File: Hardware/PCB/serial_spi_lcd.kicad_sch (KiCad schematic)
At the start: 0 parts

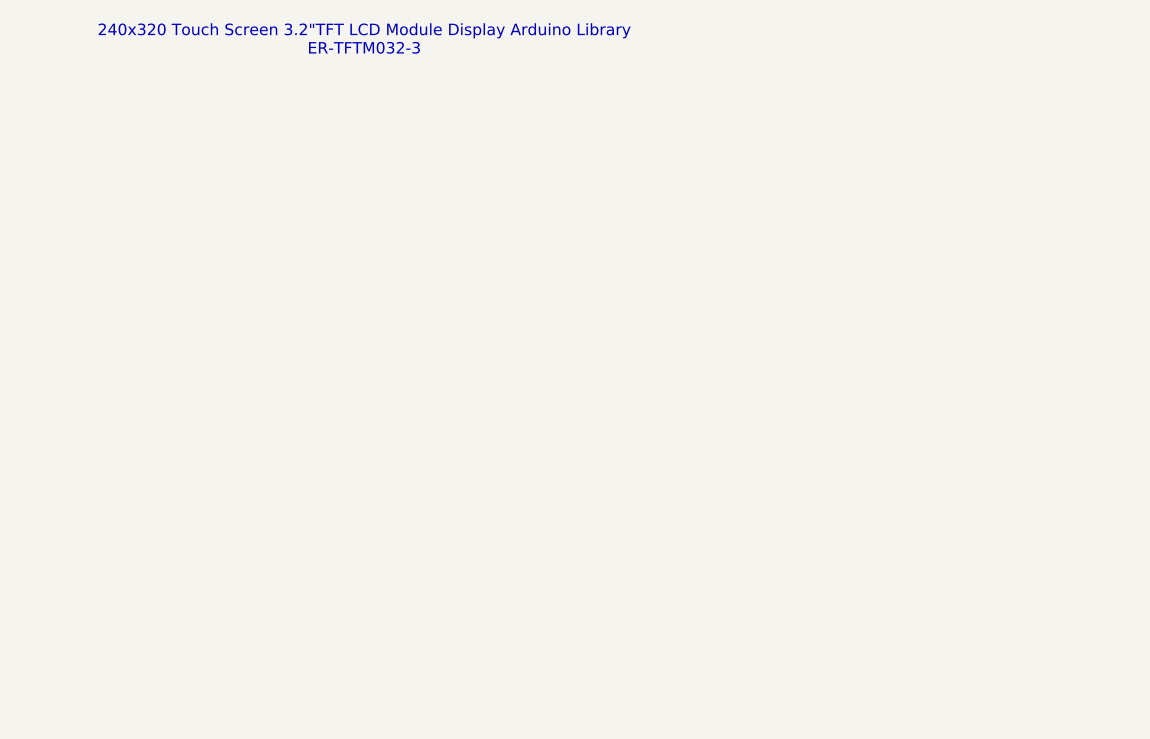
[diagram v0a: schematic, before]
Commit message: added symbol for LCD, working on adding PWM output terminal for brushless pump motors
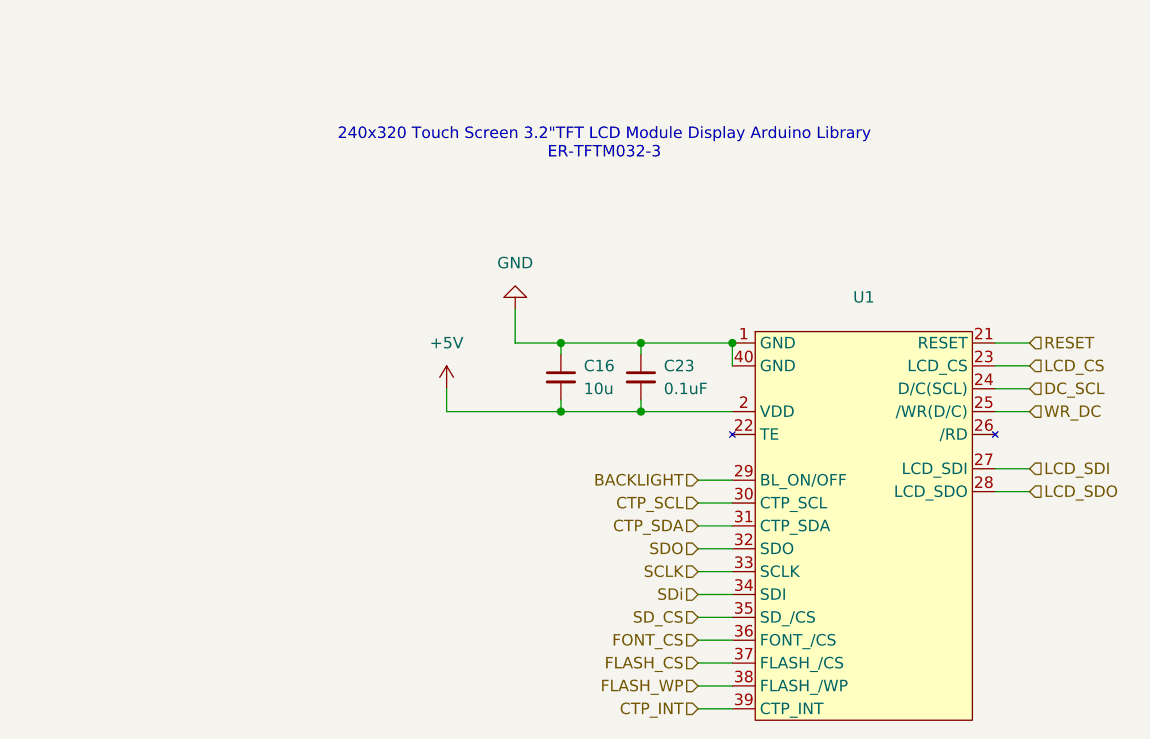
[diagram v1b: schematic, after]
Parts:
- added C16: 10u, Capacitor_SMD:C_0805_2012Metric_Pad1.18x1.45mm_HandSolder, symbol Device:C_Small
- added C23: 0.1uF, Capacitor_SMD:C_0603_1608Metric_Pad1.08x0.95mm_HandSolder, symbol Device:C_Small
- added U1: ~, Vendor_Footprints:GCT_FFC3B07-40-T, symbol Vendor_Symbols:ER-TFTM032-3
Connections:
- new net: U1.10 (DB7), U1.11 (DB8), U1.12 (DB9), U1.13 (DB10), U1.14 (DB11), U1.15 (DB12), U1.16 (DB13), U1.17 (DB14), U1.18 (DB15), U1.19 (NC), U1.20 (NC), U1.3 (DB0), U1.4 (DB1), U1.5 (DB2), U1.6 (DB3), U1.7 (DB4), U1.8 (DB5), U1.9 (DB6)
- new net +5V: C16.2, C23.2, U1.2 (VDD)
- new net BACKLIGHT: U1.29 (BL_ON/OFF)
- new net CTP_INT: U1.39 (CTP_INT)
- new net CTP_SCL: U1.30 (CTP_SCL)
- new net CTP_SDA: U1.31 (CTP_SDA)
- new net DC_SCL: U1.24 (D/C(SCL))
- new net FLASH_CS: U1.37 (FLASH_/CS)
- new net FLASH_WP: U1.38 (FLASH_/WP)
- new net FONT_CS: U1.36 (FONT_/CS)
- new net GND: C16.1, C23.1, U1.1 (GND), U1.40 (GND)
- new net LCD_CS: U1.23 (LCD_CS)
- new net LCD_SDI: U1.27 (LCD_SDI)
- new net LCD_SDO: U1.28 (LCD_SDO)
- new net RESET: U1.21 (RESET)
- new net SCLK: U1.33 (SCLK)
- new net SDO: U1.32 (SDO)
- new net SD_CS: U1.35 (SD_/CS)
- new net SDi: U1.34 (SDI)
- new net WR_DC: U1.25 (/WR(D/C))

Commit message: Added brushless DC support, fixed terminal blocks too
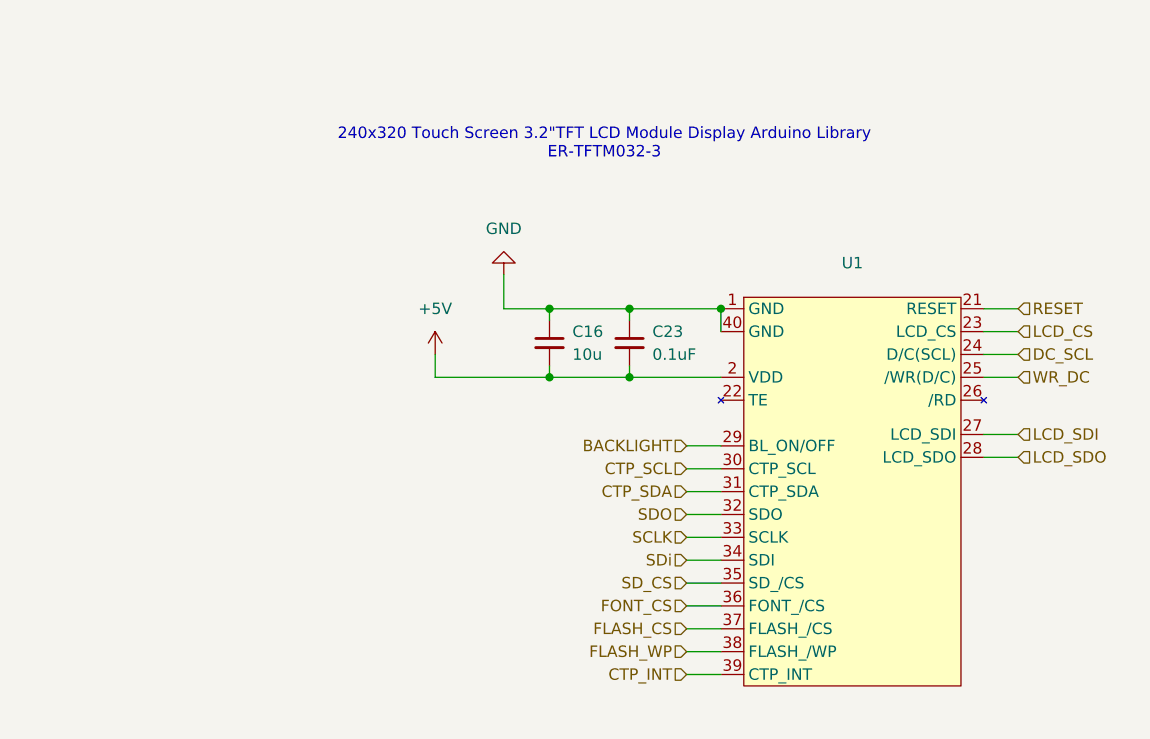
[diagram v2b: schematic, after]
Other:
- moved on the sheet: C16, C23, U1

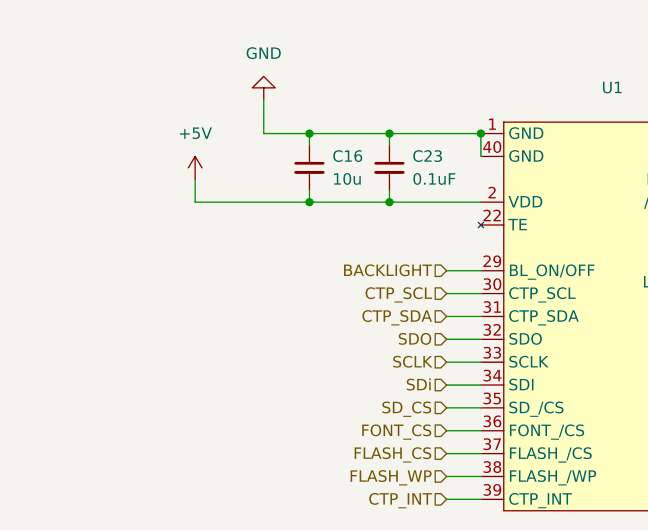
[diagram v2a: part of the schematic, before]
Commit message: switched to making buck converter to save costs and space, and to allow for LDO after 5.5V for better stability
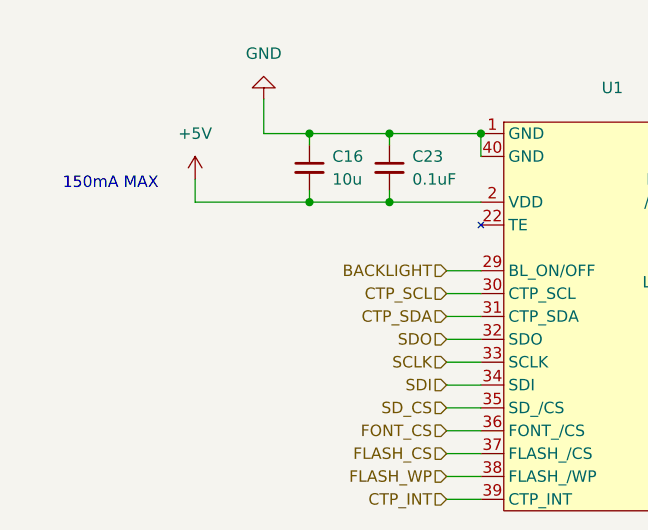
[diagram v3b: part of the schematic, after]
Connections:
- net SDi renamed SDI
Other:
- note added: "150mA MAX"

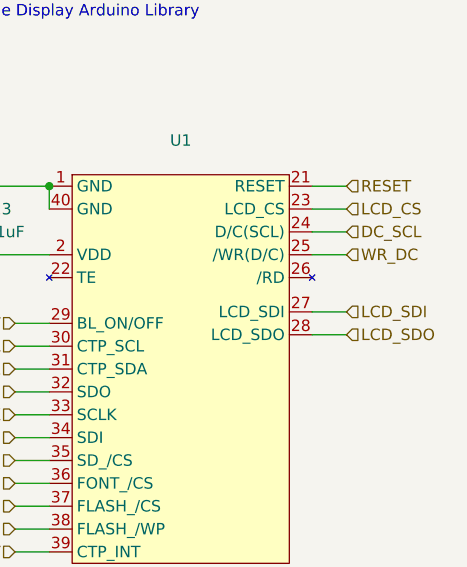
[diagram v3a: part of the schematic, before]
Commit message: consolidated IO for LCD block, broke out hierarchial pins, need to start wiring everything up and then on to layout
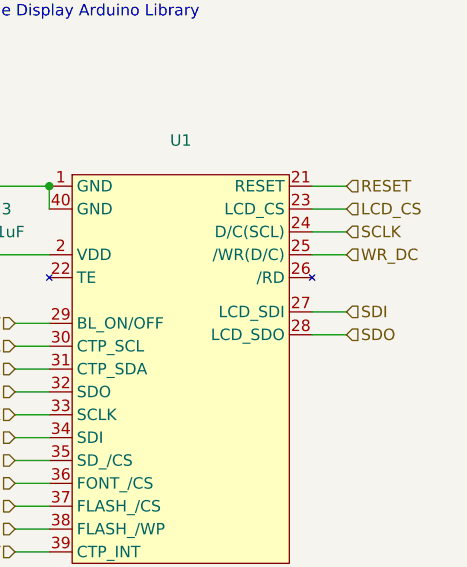
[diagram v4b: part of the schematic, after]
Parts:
- U1: DigiKey Link (none) -> https://www.digikey.com/en/products/detail/gct/FFC3B07-40-T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; MPN (none) -> FFC3B07-40-T; Manufacturer (none) -> GCT
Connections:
- net DC_SCL is gone; now on net SCLK: U1.24 (D/C(SCL))
- net LCD_SDI is gone; now on net SDI: U1.27 (LCD_SDI)
- net LCD_SDO is gone; now on net SDO: U1.28 (LCD_SDO)
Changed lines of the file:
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@@
+		)
+	)
+	(hierarchical_label "SCLK"
+		(shape input)
+		(at 123.19 55.88 0)
+		(effects
+			(font
+				(size 1.27 1.27)
+			)
+			(justify left)
 		)
 	)
@@
 		)
 	)
-	(hierarchical_label "LCD_SDO"
+	(hierarchical_label "BACKLIGHT"
+		(shape input)
+		(at 86.36 66.04 180)
+		(effects
+			(font
+				(size 1.27 1.27)
+			)
+			(justify right)
+		)
+	)
+	(hierarchical_label "FLASH_WP"
+		(shape input)
+		(at 86.36 88.9 180)
+		(effects
+			(font
+				(size 1.27 1.27)
+			)
+			(justify right)
+		)
+	)
+	(hierarchical_label "SD_CS"
+		(shape input)
+		(at 86.36 81.28 180)
+		(effects
+			(font
+				(size 1.27 1.27)
+			)
+			(justify right)
+		)
+	)
+	(hierarchical_label "CTP_SDA"
+		(shape input)
+		(at 86.36 71.12 180)
+		(effects
+			(font
+				(size 1.27 1.27)
+			)
+			(justify right)
+		)
+	)
+	(hierarchical_label "SDO"
 		(shape input)
 		(at 123.19 67.31 0)
@@
 		)
 	)
-	(hierarchical_label "BACKLIGHT"
-		(shape input)
-		(at 86.36 66.04 180)
-		(effects
-			(font
-				(size 1.27 1.27)
-			)
-			(justify right)
-		)
-	)
-	(hierarchical_label "FLASH_WP"
-		(shape input)
-		(at 86.36 88.9 180)
-		(effects
-			(font
-				(size 1.27 1.27)
-			)
-			(justify right)
-		)
-	)
-	(hierarchical_label "SD_CS"
-		(shape input)
-		(at 86.36 81.28 180)
-		(effects
-			(font
-				(size 1.27 1.27)
-			)
-			(justify right)
-		)
-	)
-	(hierarchical_label "CTP_SDA"
-		(shape input)
-		(at 86.36 71.12 180)
-		(effects
-			(font
-				(size 1.27 1.27)
-			)
-			(justify right)
+	(hierarchical_label "SDI"
+		(shape input)
+		(at 123.19 64.77 0)
+		(effects
+			(font
+				(size 1.27 1.27)
+			)
+			(justify left)
 		)
 	)
@@
 			)
 			(justify right)
-		)
-	)
-	(hierarchical_label "LCD_SDI"
-		(shape input)
-		(at 123.19 64.77 0)
-		(effects
-			(font
-				(size 1.27 1.27)
-			)
-			(justify left)
-		)
-	)
-	(hierarchical_label "DC_SCL"
-		(shape input)
-		(at 123.19 55.88 0)
-		(effects
-			(font
-				(size 1.27 1.27)
-			)
-			(justify left)
 		)
 	)
@@
 			)
 		)
-		(property "Description" ""
+		(property "Description" "40 Position FFC, FPC Connector Contacts, Bottom 0.039\" (1.00mm) Surface Mount, Right Angle"
 			(at 92.71 50.8 0)
 			(effects
 				(font
+					(size 1.27 1.27)
+				)
+				(hide yes)
+			)
+		)
+		(property "MPN" "FFC3B07-40-T"
+			(at 104.14 49.53 0)
+			(effects
+				(font
+					(size 1.27 1.27)
+				)
+				(hide yes)
+			)
+		)
+		(property "Manufacturer" "GCT"
+			(at 104.14 49.53 0)
+			(effects
+				(font
+					(size 1.27 1.27)
+				)
+				(hide yes)
+			)
+		)
+		(property "DigiKey Link" "https://www.digikey.com/en/products/detail/gct/FFC3B07-40-T/10656983"
+			(at 104.14 49.53 0)
+			(effects
+				(font
+					(size 1.27 1.27)
+				)
+				(hide yes)
+			)
+		)
+		(property "Mouser Link" ""
+			(at 104.14 49.53 0)
+			(effects
+				(font

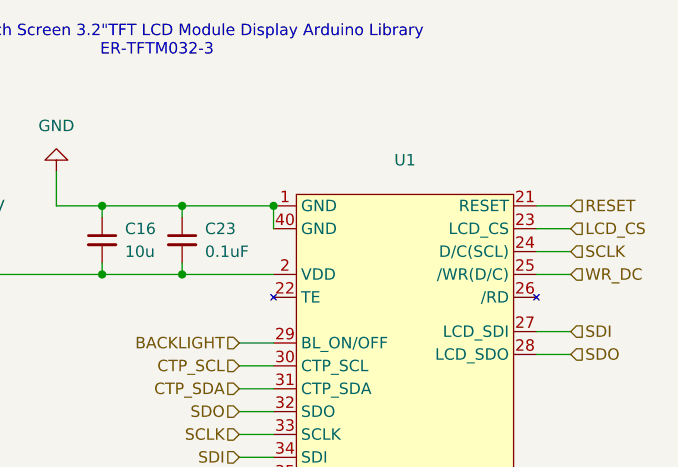
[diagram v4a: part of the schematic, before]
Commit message: overall design is pretty much done, starting layout and routing now
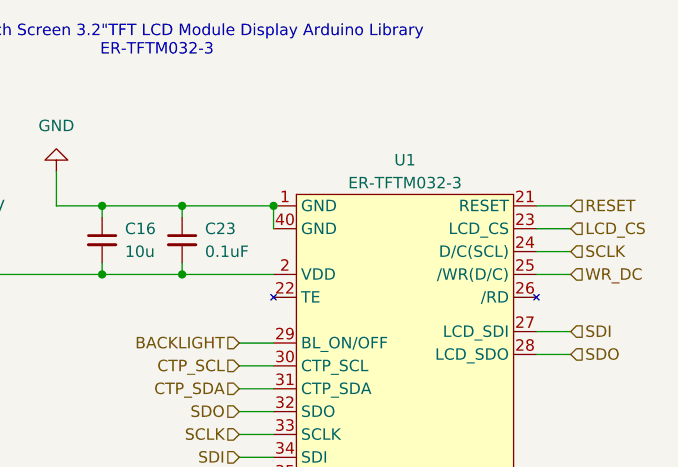
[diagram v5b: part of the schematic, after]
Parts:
- U1: value ~ -> ER-TFTM032-3

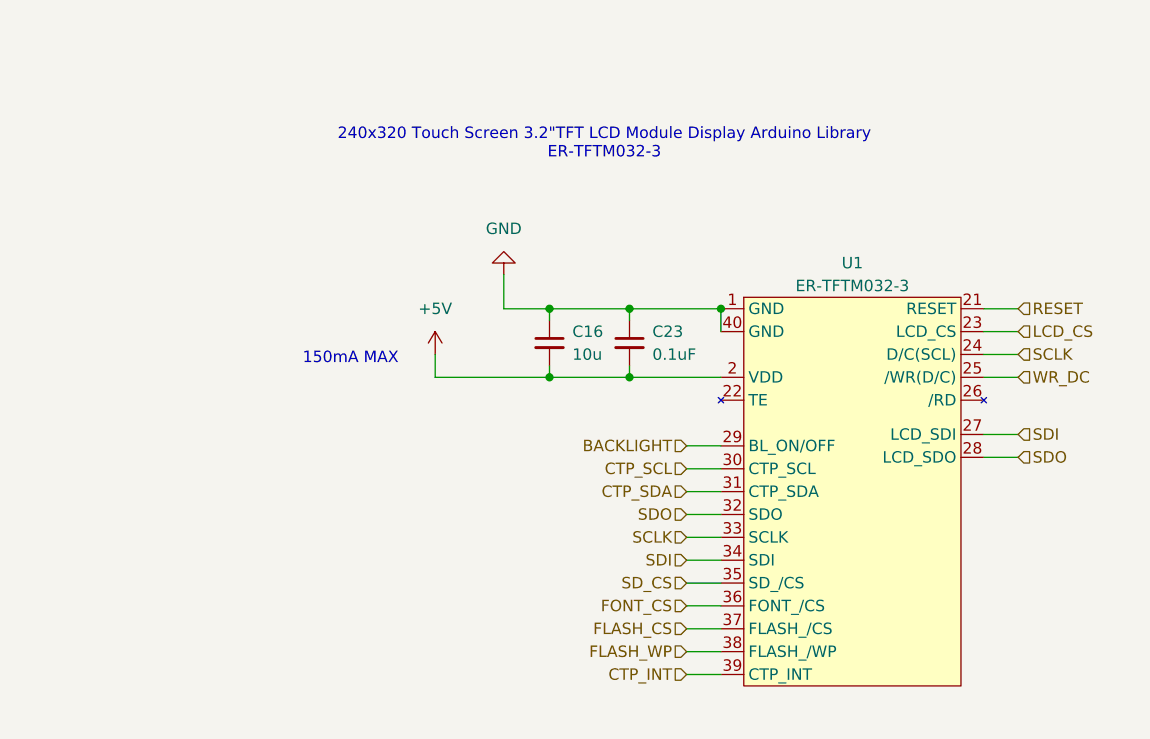
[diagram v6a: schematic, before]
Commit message: fixed BOM, added some silkscreen, getting quote now
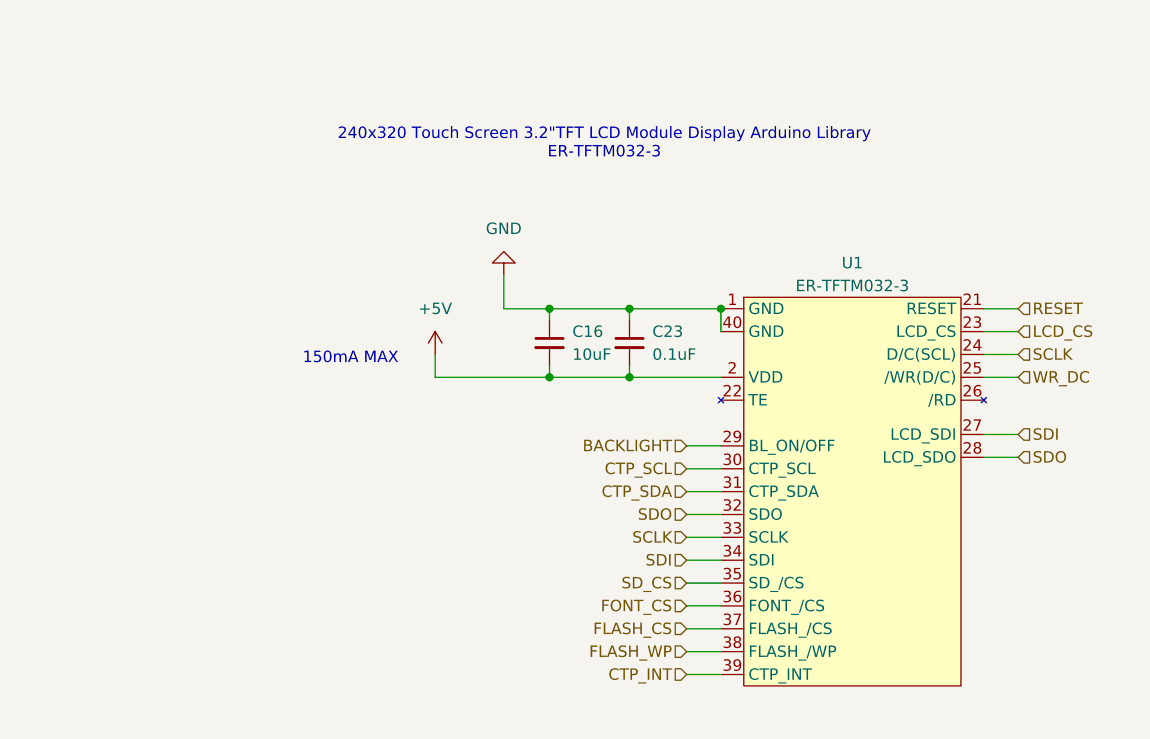
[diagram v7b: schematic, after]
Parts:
- C16: value 10u -> 10uF
- C23: DigiKey Link (none) -> https://www.digikey.com/en/products/detail/samsung-electro-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; MPN GCM188R71H104KA57J -> CL10B104KO8NNNC; Manufacturer (none) -> Samsung Electro-Mechanics
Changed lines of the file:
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@@
 			"AHoAdQBnAHIAWQB6AC8AVwBHACsAYgBoAEYANgBGAGoAMQA3ADEAMQArAGoAcQBOADgAZQBRAHcA"
 			"ZQBaAFEASQAxAGIAQQAzADEAWABiAE0ASAAyAEkAeQA1AFkAWgBYAHcAWABzAC8AdQBPAHgAZgBG"
-			"AFAAZwBxAE8ANQBsAEQAYQBhAEQAKwAwAEoAQQA0AG4AcwBzAFoAQQBLAGwAWABnAA=="
+			"AFAAZwBxAE8ANQBsAEQAYQBhAEQAKwAwAEoAQQA0AG4AcwBzAFoAQQBLAGwAWABnAAAAEBs6AXIC"
+			"AACQVToBcgIAAIidSp/7fwAAkLtKn/t/AACInUqf+38AAMBVOgFyAgAAMBs6AXICAAAwvkqf+38A"
+			"AFAbOgFyAgAA8FU6AXICAACInUqf+38AAJC7Sp/7fwAAiJ1Kn/t/AAAgVjoBcgIAAHAbOgFyAgAA"
+			"ML5Kn/t/AACQGzoBcgIAAFBWOgFyAgAAiJ1Kn/t/AACQu0qf+38AAIidSp/7fwAAgFY6AXICAACw"
+			"GzoBcgIAADC+Sp/7fwAA0Bs6AXICAACwVjoBcgIAAIidSp/7fwAAkLtKn/t/AACInUqf+38AAOBW"
+			"OgFyAgAA8Bs6AXICAAAwvkqf+38AABAcOgFyAgAAEFc6AXICAACInUqf+38AAJC7Sp/7fwAAiJ1K"
+			"n/t/AABAVzoBcgIAADAcOgFyAgAAML5Kn/t/AABQHDoBcgIAAHBXOgFyAgAAiJ1Kn/t/AACQu0qf"
+			"+38AAIidSp/7fwAAoFc6AXICAABwHDoBcgIAADC+Sp/7fwAAkBw6AXICAADQVzoBcgIAAIidSp/7"
+			"fwAAkLtKn/t/AACInUqf+38AAABYOgFyAgAAsBw6AXICAAAwvkqf+38AANAcOgFyAgAAMFg6AXIC"
+			"AACInUqf+38AAJC7Sp/7fwAAiJ1Kn/t/AABgWDoBcgIAAPAcOgFyAgAAML5Kn/t/AAAQHToBcgIA"
+			"AJBYOgFyAgAAiJ1Kn/t/AACQu0qf+38AAIidSp/7fwAAwFg6AXICAAAwHToBcgIAADC+Sp/7fwAA"
+			"UB06AXICAADwWDoBcgIAAIidSp/7fwAAkLtKn/t/AACInUqf+38AACBZOgFyAgAAcB06AXICAAAw"
+			"vkqf+38AAJAdOgFyAgAAUFk6AXICAACInUqf+38AAJC7Sp/7fwAAiJ1Kn/t/AACAWToBcgIAALAd"
+			"OgFyAgAAML5Kn/t/AADQHToBcgIAALBZOgFyAgAAiJ1Kn/t/AACQu0qf+38AAIidSp/7fwAA4Fk6"
+			"AXICAADwHToBcgIAADC+Sp/7fwAAEB46AXICAAAQWjoBcgIAAIidSp/7fwAAkLtKn/t/AACInUqf"
+			"+38AAEBaOgFyAgAAMB46AXICAAAwvkqf+38AAFAeOgFyAgAAcFo6AXICAACInUqf+38AAJC7Sp/7"
+			"fwAAiJ1Kn/t/AACgWjoBcgIAAHAeOgFyAgAAML5Kn/t/AACQHjoBcgIAANBaOgFyAgAAiJ1Kn/t/"
+			"AACQu0qf+38AAIidSp/7fwAAAFs6AXICAACwHjoBcgIAADC+Sp/7fwAA0B46AXICAAAwWzoBcgIA"
+			"AIidSp/7fwAAkLtKn/t/AACInUqf+38AAGBbOgFyAgAA8B46AXICAAAwvkqf+38AAA=="
 		)
 	)
@@
 			)
 		)
-		(property "Description" "0.1 µF ±10% 50V Ceramic Capacitor X7R 0603 (1608 Metric)"
-			(at 80.01 54.61 0)
-			(effects
-				(font
-					(size 1.27 1.27)
-				)
-				(hide yes)
-			)
-		)
-		(property "MPN" "GCM188R71H104KA57J"
+		(property "Description" "0.1 µF ±10% 16V Ceramic Capacitor X7R 0603 (1608 Metric)"
+			(at 80.01 54.61 0)
+			(effects
+				(font
+					(size 1.27 1.27)
+				)
+				(hide yes)
+			)
+		)
+		(property "MPN" "CL10B104KO8NNNC"
+			(at 80.01 54.61 0)
+			(effects
+				(font
+					(size 1.27 1.27)
+				)
+				(hide yes)
+			)
+		)
+		(property "DigiKey Link" "https://www.digikey.com/en/products/detail/samsung-electro-mechanics/CL10B104KO8NNNC/3886663"
+			(at 80.01 54.61 0)
+			(effects
+				(font
+					(size 1.27 1.27)
+				)
+				(hide yes)
+			)
+		)
+		(property "Manufacturer" "Samsung Electro-Mechanics"
+			(at 80.01 54.61 0)
+			(effects
+				(font
+					(size 1.27 1.27)
+				)
+				(hide yes)
+			)
+		)
+		(property "Mouser Link" ""
 			(at 80.01 54.61 0)
 			(effects
@@
 			)
 		)
-		(property "Value" "10u"
+		(property "Value" "10uF"
 			(at 73.66 55.8862 0)
 			(effects
